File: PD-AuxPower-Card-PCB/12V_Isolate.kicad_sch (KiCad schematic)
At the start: 33 parts, among them J4 2.54mm terminal, Q1 FDMC86520L, T1 EFD10, U12 TL431DBZ, U7 EL3H7(C)(TA)-G

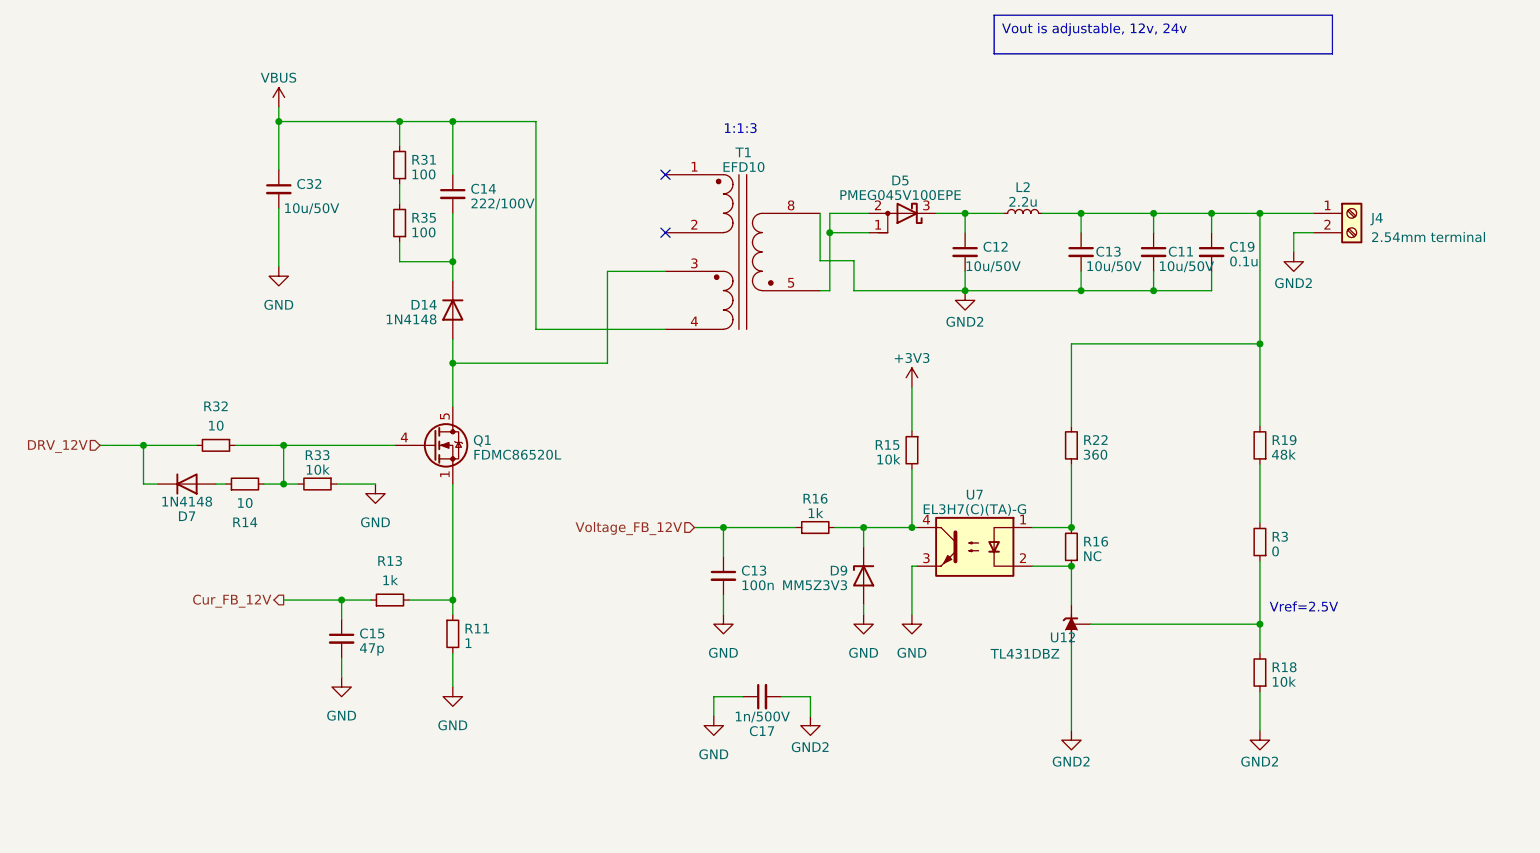
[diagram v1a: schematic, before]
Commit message: FEAT: Change PWM frequency to 50kHz, fix LED indicator bug PCB FIX: Adjust ophotocoupler feedback resistor value
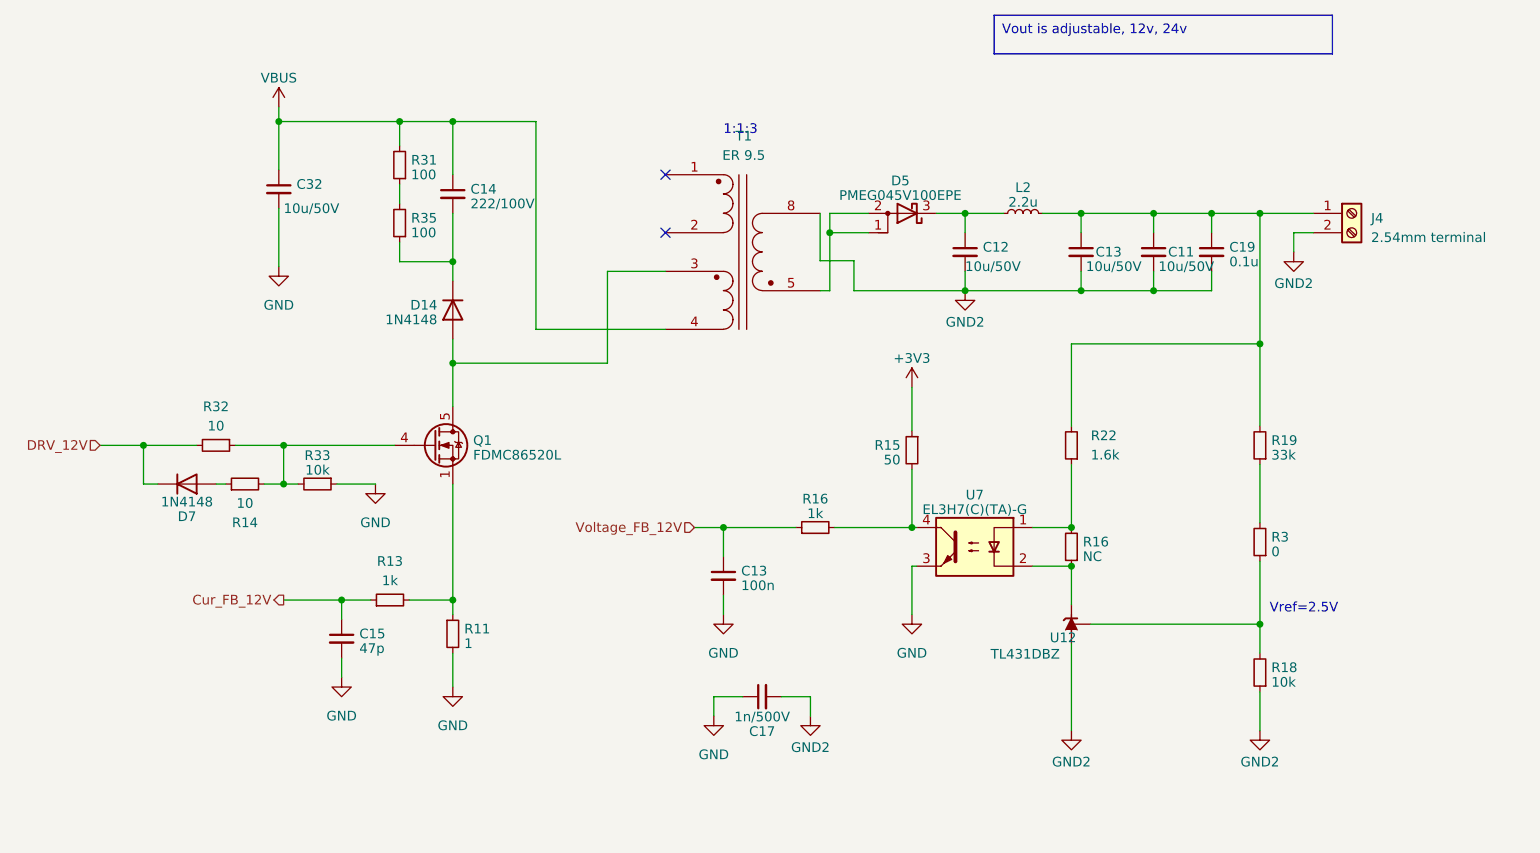
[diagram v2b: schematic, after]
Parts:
- removed D9: MM5Z3V3, Diode_SMD:D_SOD-523, symbol Diode:BZV55B3V3
- R15: value 10k -> 50
- R19: value 48k -> 33k
- R22: value 360 -> 1.6k
- T1: value EFD10 -> ER 9.5
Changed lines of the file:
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@@
   (junction (at 77.47 91.44) (diameter 0) (color 0 0 0 0)
-  )
-  (junction (at 172.085 102.235) (diameter 0) (color 0 0 0 0)
   )
   (junction (at 200.66 60.96) (diameter 0) (color 0 0 0 0)
@@
     (stroke (width 0) (type default))
   )
-  (wire (pts (xy 168.275 102.235) (xy 172.085 102.235))
+  (wire (pts (xy 168.275 102.235) (xy 178.435 102.235))
     (stroke (width 0) (type default))
   )
@@
     (stroke (width 0) (type default))
   )
-  (wire (pts (xy 172.085 102.235) (xy 178.435 102.235))
-    (stroke (width 0) (type default))
-  )
   (wire (pts (xy 118.11 60.96) (xy 118.11 67.31))
     (stroke (width 0) (type default))
@@
     (stroke (width 0) (type default))
   )
-  (wire (pts (xy 172.085 112.395) (xy 172.085 113.665))
-    (stroke (width 0) (type default))
-  )
   (wire (pts (xy 95.885 91.44) (xy 110.49 91.44))
     (stroke (width 0) (type default))
@@
   )
   (wire (pts (xy 170.815 67.183) (xy 170.815 71.12))
-    (stroke (width 0) (type default))
-  )
-  (wire (pts (xy 172.085 104.775) (xy 172.085 102.235))
     (stroke (width 0) (type default))
   )
@@
       (effects (font (size 1.27 1.27)) (justify left))
     )
-    (property "Value" "10k" (at 176.9364 93.3523 0)
+    (property "Value" "50" (at 176.9364 93.3523 0)
       (effects (font (size 1.27 1.27)) (justify left))
     )
@@
         (path "/48c5bc14-ccc3-44de-b526-838e3d53c0ee/9a44a331-fce1-4dee-b5a9-6d547d8c4b08"
           (reference "C29") (unit 1)
-        )
-      )
-    )
-  )
-  (symbol (lib_id "Diode:BZV55B3V3") (at 172.085 108.585 90) (mirror x) (unit 1)
-    (in_bom yes) (on_board yes) (dnp no)
-    (property "Reference" "D9" (at 170.053 107.9413 90)
-      (effects (font (size 1.27 1.27)) (justify left))
-    )
-    (property "Value" "MM5Z3V3" (at 170.053 109.8623 90)
-      (effects (font (size 1.27 1.27)) (justify left))
-    )
-    (property "Footprint" "Diode_SMD:D_SOD-523" (at 176.53 108.585 0)
-      (effects (font (size 1.27 1.27)) hide)
-    )
-    (property "Datasheet" "https://assets.nexperia.com/documents/data-sheet/BZV55_SER.pdf" (at 172.085 108.585 0)
-      (effects (font (size 1.27 1.27)) hide)
-    )
-    (pin "1")
-    (pin "2")
-    (instances
-      (project "PD-AuxPower-Card"
-        (path "/48c5bc14-ccc3-44de-b526-838e3d53c0ee/40f113c1-6183-4863-b2ec-a4ca33698158"
-          (reference "D9") (unit 1)
-        )
-        (path "/48c5bc14-ccc3-44de-b526-838e3d53c0ee/9a44a331-fce1-4dee-b5a9-6d547d8c4b08"
-          (reference "D20") (unit 1)
         )
       )
@@
   (symbol (lib_id "Device:R_Small") (at 199.39 91.44 180) (unit 1)
     (in_bom yes) (on_board yes) (dnp no) (fields_autoplaced)
-    (property "Reference" "R22" (at 200.8886 90.7963 0)
+    (property "Reference" "R22" (at 201.93 90.17 0)
       (effects (font (size 1.27 1.27)) (justify right))
     )
-    (property "Value" "360" (at 200.8886 92.7173 0)
+    (property "Value" "1.6k" (at 201.93 92.71 0)
       (effects (font (size 1.27 1.27)) (justify right))
     )
@@
       (effects (font (size 1.27 1.27)) (justify right))
     )
-    (property "Value" "48k" (at 225.6536 92.7173 0)
+    (property "Value" "33k" (at 225.6536 92.7173 0)
       (effects (font (size 1.27 1.27)) (justify right))
     )
@@
   (symbol (lib_id "Device:Transformer_1P_2S") (at 156.21 66.04 0) (mirror y) (unit 1)
     (in_bom yes) (on_board yes) (dnp no) (fields_autoplaced)
-    (property "Reference" "T1" (at 156.337 52.9969 0)
-      (effects (font (size 1.27 1.27)))
-    )
-    (property "Value" "EFD10" (at 156.337 54.9179 0)
+    (property "Reference" "T1" (at 156.337 50.8 0)
+      (effects (font (size 1.27 1.27)))
+    )
+    (property "Value" "ER 9.5" (at 156.337 53.34 0)
       (effects (font (size 1.27 1.27)))
     )
@@
         )
       )
-    )
-  )
-  (symbol (lib_id "power:GND") (at 172.085 113.665 0) (unit 1)
-    (in_bom yes) (on_board yes) (dnp no) (fields_autoplaced)
-    (property "Reference" "#PWR08" (at 172.085 120.015 0)
-      (effects (font (size 1.27 1.27)) hide)
-    )
-    (property "Value" "GND" (at 172.085 118.745 0)
-      (effects (font (size 1.27 1.27)))
-    )
-    (property "Footprint" "" (at 172.085 113.665 0)
-      (effects (font (size 1.27 1.27)) hide)
-    )
-    (property "Datasheet" "" (at 172.085 113.665 0)
-      (effects (font (size 1.27 1.27)) hide)
-    )
-    (pin "1")
-    (instances
-      (project "PD-AuxPower-Card"
-        (path "/48c5bc14-ccc3-44de-b526-838e3d53c0ee"
-          (reference "#PWR08") (unit 1)
-        )
-        (path "/48c5bc14-ccc3-44de-b526-838e3d53c0ee/40f113c1-6183-4863-b2ec-a4ca33698158"
-          (reference "#PWR049") (unit 1)
-        )
-        (path "/48c5bc14-ccc3-44de-b526-838e3d53c0ee/9a44a331-fce1-4dee-b5a9-6d547d8c4b08"
-          (reference "#PWR081") (unit 1)
-        )
-      )

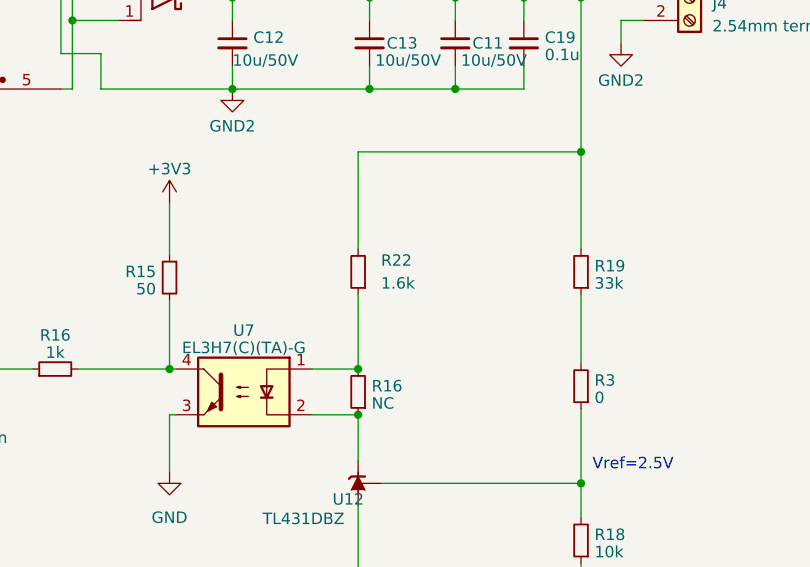
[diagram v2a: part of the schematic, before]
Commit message: FEAT: Add PID algorithm for output voltage control. NOT TUNE YET! Change ADC1 trigger source into TIM1 TRGO for update event. Synchronised TIM2 and TIM1 by using slave mode. PCB: Change TL431 to TLV431 for 3.3V output rail. Change some tuned resistor value for next sample.
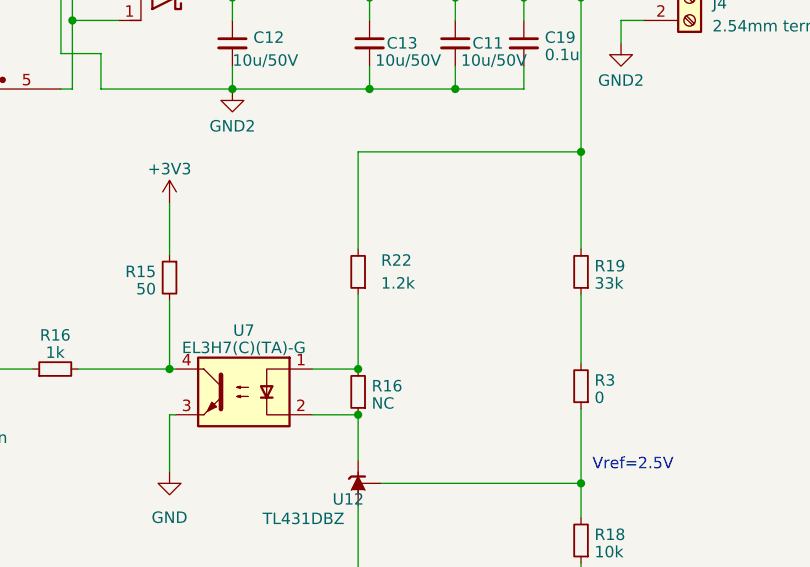
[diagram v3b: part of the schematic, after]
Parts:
- R22: value 1.6k -> 1.2k
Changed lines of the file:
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@@
       (effects (font (size 1.27 1.27)) (justify right))
     )
-    (property "Value" "1.6k" (at 201.93 92.71 0)
+    (property "Value" "1.2k" (at 201.93 92.71 0)
       (effects (font (size 1.27 1.27)) (justify right))
     )

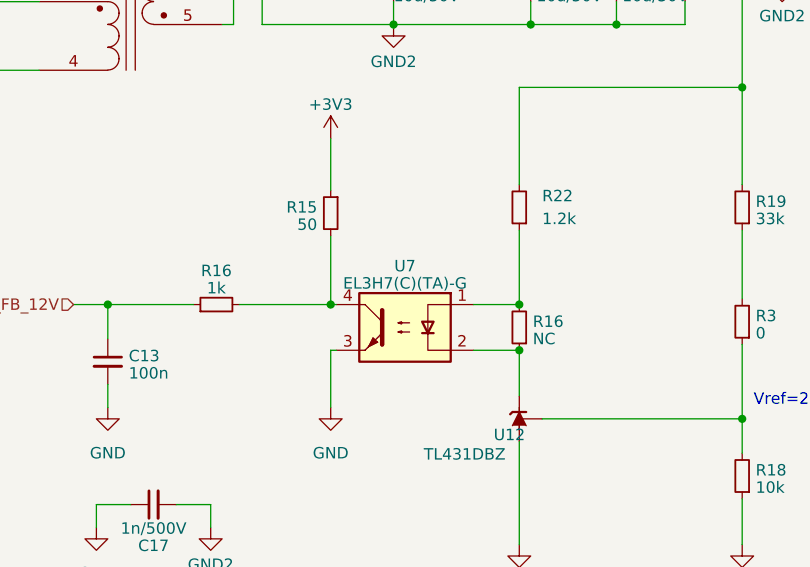
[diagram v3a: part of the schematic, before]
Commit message: PCB: Update LTV-214 footprint and update to PCB layout.
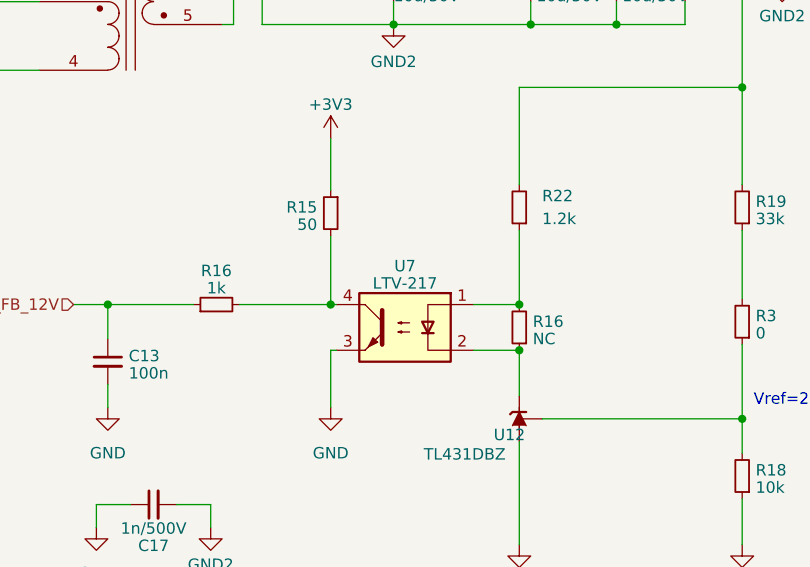
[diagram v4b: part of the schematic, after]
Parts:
- U7: value EL3H7(C)(TA)-G -> LTV-217; footprint OptoDevice:Panasonic_APV-AQY_SSOP-4_4.45x2.65mm_P1.27mm -> Library:SOP-4-175mil
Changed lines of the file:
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@@
       (effects (font (size 1.27 1.27)))
     )
-    (property "Value" "EL3H7(C)(TA)-G" (at 186.69 99.8761 0)
+    (property "Value" "LTV-217" (at 186.69 99.8761 0)
       (effects (font (size 1.27 1.27)))
     )
-    (property "Footprint" "OptoDevice:Panasonic_APV-AQY_SSOP-4_4.45x2.65mm_P1.27mm" (at 191.77 109.855 0)
+    (property "Footprint" "Library:SOP-4-175mil" (at 191.77 109.855 0)
       (effects (font (size 1.27 1.27) italic) (justify left) hide)
     )

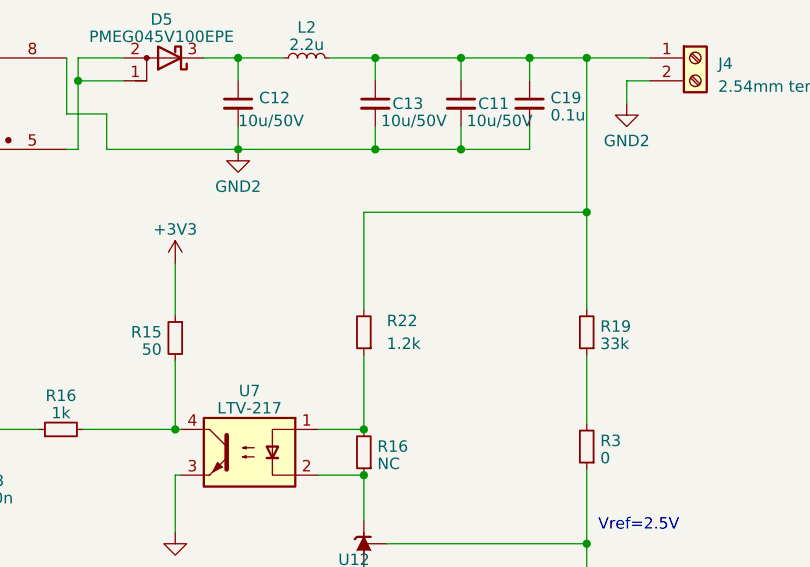
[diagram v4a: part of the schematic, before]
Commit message: FEAT: Increase PWM frequency to 200kHz, add PD protocol lib prototype. PCB: Add comment of 12/24V feedback loop. Doc: Change technical reference manual for STM32L4xx
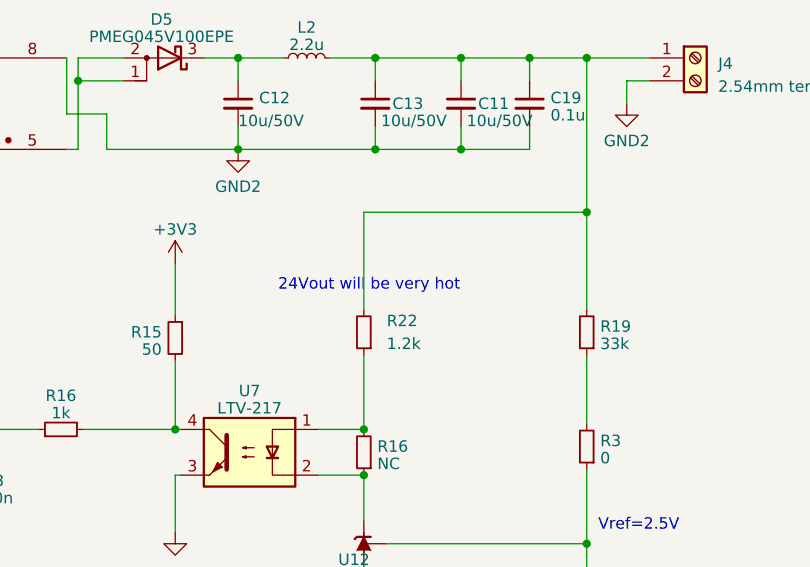
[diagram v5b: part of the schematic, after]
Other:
- note added: "24Vout will be very hot"
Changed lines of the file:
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@@
+    (effects (font (size 1.27 1.27)) (justify left bottom))
+  )
+  (text "24Vout will be very hot" (at 189.865 86.995 0)
     (effects (font (size 1.27 1.27)) (justify left bottom))
   )
